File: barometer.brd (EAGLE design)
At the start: 58.4 x 40.4 mm, 103 parts, among them IC1 TPS5410, IC2 ZPA2326-0311A-R, IC3 MIC5225-3.3v, Q1 BC817, U1 LTC2850, U2 PCA9306, U3 DAC8574, U4 XTR117, U5 XC6215XC6215B182NR, U6 MAX3221, U7 Tiny85-20-SMT, X1 1751248, X2 1751264

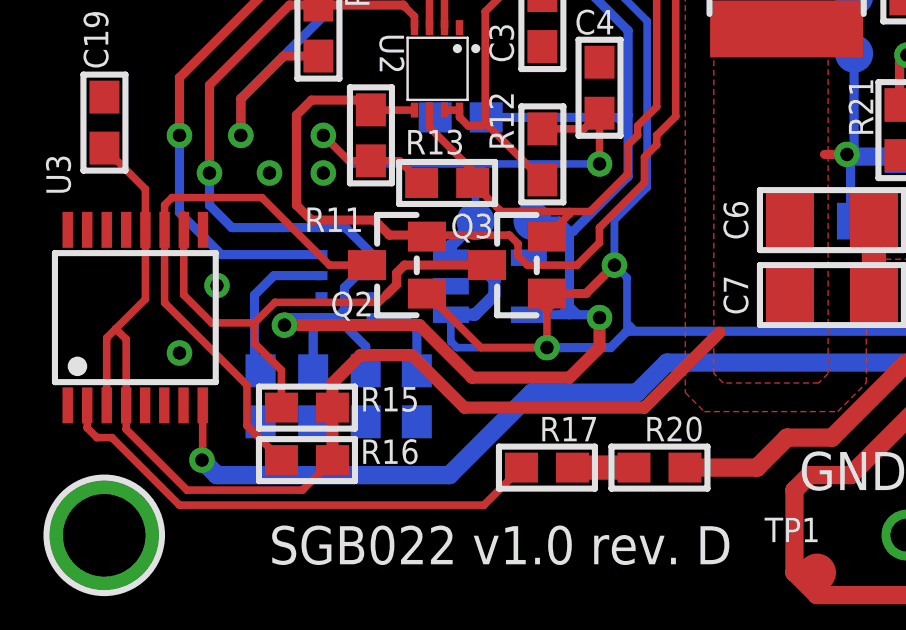
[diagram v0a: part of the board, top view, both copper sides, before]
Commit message: Optimize via placement and routing
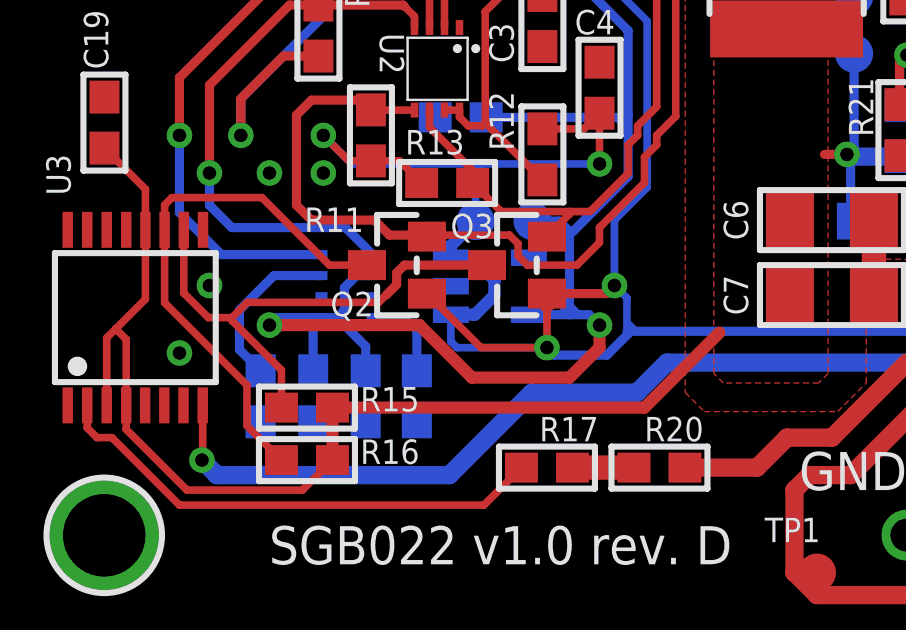
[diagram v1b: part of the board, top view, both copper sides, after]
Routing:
- net +5V0: track 47.2 -> 45.2 mm
- net +1V8: track 80.4 -> 81.3 mm
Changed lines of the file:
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@@
 <via x="17.4025" y="23.0825" extent="1-16" drill="0.45"/>
 <via x="54.88" y="6.7525" extent="1-16" drill="0.45"/>
-<via x="7.25" y="11.82" extent="1-16" drill="0.45"/>
+<via x="7" y="11.82" extent="1-16" drill="0.45"/>
 </signal>
 <signal name="+5V0">
@@
 <contactref element="R16" pad="2"/>
 <contactref element="R15" pad="2"/>
-<wire x1="13.75" y1="9.5" x2="15.5" y2="7.75" width="0.4064" layer="1"/>
-<wire x1="15.5" y1="7.75" x2="21.5" y2="7.75" width="0.4064" layer="1"/>
-<wire x1="21.5" y1="7.75" x2="24" y2="10.25" width="0.4064" layer="1"/>
-<wire x1="13.75" y1="9.5" x2="12.035" y2="9.5" width="0.4064" layer="1"/>
+<wire x1="24" y1="10.25" x2="21.5" y2="7.75" width="0.4064" layer="1"/>
 <wire x1="30.0075" y1="16.1175" x2="28.3225" y2="16.1175" width="0.6096" layer="16"/>
 <wire x1="28.3225" y1="16.1175" x2="28.25" y2="16.19" width="0.6096" layer="16"/>
@@
 <contactref element="U3" pad="4"/>
 <contactref element="C19" pad="1"/>
-<wire x1="12.035" y1="9.5" x2="11.1" y2="8.565" width="0.4064" layer="1"/>
-<wire x1="11.1" y1="8.565" x2="11.1" y2="7.75" width="0.4064" layer="1"/>
 <wire x1="11.1" y1="7.75" x2="11.1" y2="6" width="0.4064" layer="1"/>
 <wire x1="4.865" y1="13.675" x2="4.865" y2="11.365" width="0.254" layer="1"/>
@@
 <wire x1="3.5" y1="16.4" x2="4.865" y2="15.035" width="0.254" layer="1"/>
 <wire x1="4.865" y1="15.035" x2="4.865" y2="13.675" width="0.254" layer="1"/>
+<wire x1="21.5" y1="7.75" x2="11.1" y2="7.75" width="0.4064" layer="1"/>
 </signal>
 <signal name="B1">
@@
 <wire x1="16.1925" y1="26.25" x2="16.1925" y2="26.4897" width="0.254" layer="16"/>
 <wire x1="16.6225" y1="24.3775" x2="16.1925" y2="24.8075" width="0.254" layer="16"/>
-<wire x1="18.25" y1="11.55" x2="19.55" y2="11.55" width="0.3048" layer="1"/>
-<wire x1="19.55" y1="11.55" x2="20.5" y2="12.5" width="0.3048" layer="1"/>
-<via x="20.5" y="12.5" extent="1-16" drill="0.45"/>
+<via x="20.5" y="11.82" extent="1-16" drill="0.45"/>
 <wire x1="12.5" y1="28.5" x2="13.5" y2="27.5" width="0.3048" layer="16"/>
 <wire x1="15.1822" y1="27.5" x2="16.1925" y2="26.4897" width="0.3048" layer="16"/>
 <wire x1="13.5" y1="27.5" x2="15.1822" y2="27.5" width="0.3048" layer="16"/>
-<wire x1="18.25" y1="9.75" x2="20.375" y2="9.75" width="0.3048" layer="16"/>
-<wire x1="20.375" y1="9.75" x2="20.875" y2="10.25" width="0.3048" layer="16"/>
-<wire x1="20.875" y1="10.25" x2="20.9175" y2="10.2925" width="0.3048" layer="16"/>
 <wire x1="21.59" y1="20.635" x2="21.59" y2="15.09" width="0.254" layer="16"/>
 <wire x1="21.59" y1="15.09" x2="20.5" y2="14" width="0.254" layer="16"/>
-<wire x1="20.5" y1="14" x2="20.5" y2="12.5" width="0.254" layer="16"/>
-<wire x1="20.5" y1="12.5" x2="20.9175" y2="12.0825" width="0.254" layer="16"/>
-<wire x1="20.9175" y1="12.0825" x2="20.9175" y2="10.2925" width="0.254" layer="16"/>
 <wire x1="21" y1="10.5" x2="21.125" y2="10.375" width="0.254" layer="16"/>
-<wire x1="21" y1="10.5" x2="21" y2="10.375" width="0.254" layer="16"/>
-<wire x1="21" y1="10.375" x2="20.875" y2="10.25" width="0.254" layer="16"/>
+<wire x1="21" y1="10.375" x2="21" y2="10.5" width="0.254" layer="16"/>
 <contactref element="U1" pad="8"/>
 <contactref element="R2" pad="2"/>
@@
 <wire x1="14.85" y1="26.25" x2="16.1925" y2="26.25" width="0.8128" layer="16"/>
 <wire x1="40" y1="31.4" x2="40" y2="30.16" width="0.6096" layer="1"/>
+<wire x1="20.23" y1="11.55" x2="20.5" y2="11.82" width="0.3048" layer="1"/>
+<wire x1="18.25" y1="11.55" x2="20.23" y2="11.55" width="0.3048" layer="1"/>
+<wire x1="20.5" y1="14" x2="20.5" y2="11.82" width="0.254" layer="16"/>
+<wire x1="20.9175" y1="10.2925" x2="20.9175" y2="11.4025" width="0.254" layer="16"/>
+<wire x1="20.9175" y1="11.4025" x2="20.5" y2="11.82" width="0.254" layer="16"/>
+<wire x1="18.25" y1="9.75" x2="18.5" y2="9.5" width="0.3048" layer="16"/>
+<wire x1="18.5" y1="9.5" x2="20.25" y2="9.5" width="0.3048" layer="16"/>
+<wire x1="21" y1="10.25" x2="21" y2="10.375" width="0.3048" layer="16"/>
+<wire x1="20.25" y1="9.5" x2="21" y2="10.25" width="0.3048" layer="16"/>
 </signal>
 <signal name="C1+">
@@
 <wire x1="12.2084" y1="8.9762" x2="12.2084" y2="9.7916" width="0.3048" layer="16"/>
 <wire x1="12.2084" y1="9.7916" x2="11.25" y2="10.75" width="0.3048" layer="16"/>
-<via x="20.0025" y="10.75" extent="1-16" drill="0.45"/>
-<via x="9.5" y="10.5" extent="1-16" drill="0.45"/>
-<wire x1="9.5" y1="10.5" x2="9.75" y2="10.75" width="0.3048" layer="16"/>
-<wire x1="9.75" y1="10.75" x2="10.735" y2="10.75" width="0.3048" layer="16"/>
+<via x="20.0025" y="10.5" extent="1-16" drill="0.45"/>
+<via x="9" y="10.5" extent="1-16" drill="0.45"/>
+<wire x1="9" y1="10.5" x2="9.25" y2="10.75" width="0.3048" layer="16"/>
+<wire x1="9.25" y1="10.75" x2="10.735" y2="10.75" width="0.3048" layer="16"/>
 <contactref element="U2" pad="2"/>
 <wire x1="14.835" y1="20.4175" x2="14.835" y2="22.035" width="0.254" layer="1"/>
@@
 <wire x1="9.4675" y1="19.4675" x2="10.6325" y2="19.4675" width="0.3048" layer="1"/>
 <wire x1="14" y1="10.5" x2="15.75" y2="8.75" width="0.4064" layer="1"/>
-<wire x1="14" y1="10.5" x2="9.5" y2="10.5" width="0.4064" layer="1"/>
+<wire x1="14" y1="10.5" x2="9" y2="10.5" width="0.4064" layer="1"/>
 <wire x1="17.6475" y1="10.8475" x2="19" y2="10.8475" width="0.3048" layer="16"/>
 <wire x1="17.7725" y1="13.9675" x2="18.6575" y2="13.9675" width="0.3048" layer="16"/>
@@
 <wire x1="19" y1="11.125" x2="18.75" y2="10.875" width="0.3048" layer="16"/>
 <wire x1="19" y1="11.125" x2="19.25" y2="10.875" width="0.3048" layer="16"/>
-<wire x1="20.0025" y1="9.7525" x2="20.0025" y2="10.75" width="0.4064" layer="1"/>
 <wire x1="15.75" y1="8.75" x2="19" y2="8.75" width="0.4064" layer="1"/>
 <wire x1="19" y1="8.75" x2="20.0025" y2="9.7525" width="0.4064" layer="1"/>
 <wire x1="20.955" y1="17.5" x2="20.955" y2="15.455" width="0.3048" layer="16"/>
-<wire x1="19.905" y1="10.8475" x2="20.0025" y2="10.75" width="0.3048" layer="16"/>
-<wire x1="19" y1="10.8475" x2="19.905" y2="10.8475" width="0.3048" layer="16"/>
+<wire x1="19" y1="10.8475" x2="19.655" y2="10.8475" width="0.3048" layer="16"/>
 <wire x1="11.1125" y1="21.5875" x2="9.7275" y2="22.9725" width="0.3048" layer="16"/>
 <wire x1="9.7275" y1="22.9725" x2="9.7275" y2="25.5875" width="0.3048" layer="16"/>
@@
 <wire x1="19.125" y1="13.625" x2="19" y2="13.625" width="0.3048" layer="16"/>
 <wire x1="20.955" y1="15.455" x2="19.125" y2="13.625" width="0.3048" layer="16"/>
+<wire x1="20.0025" y1="9.7525" x2="20.0025" y2="10.5" width="0.4064" layer="1"/>
+<wire x1="19.655" y1="10.8475" x2="20.0025" y2="10.5" width="0.3048" layer="16"/>
 </signal>
 <signal name="VREF_3V3">
@@
 <contactref element="IC2" pad="3"/>
 <contactref element="R19" pad="1"/>
-<wire x1="10.735" y1="12.15" x2="9.15" y2="12.15" width="0.3048" layer="16"/>
-<wire x1="9.15" y1="12.15" x2="8.5" y2="11.5" width="0.3048" layer="16"/>
-<wire x1="8.5" y1="11.5" x2="8.5" y2="9.1823" width="0.3048" layer="16"/>
-<wire x1="8.5" y1="9.1823" x2="8.7061" y2="8.9762" width="0.3048" layer="16"/>
+<wire x1="9.15" y1="12.15" x2="10.735" y2="12.15" width="0.3048" layer="16"/>
+<wire x1="8.7061" y1="8.9762" x2="8" y2="9.6823" width="0.3048" layer="16"/>
+<wire x1="8" y1="11" x2="9.15" y2="12.15" width="0.3048" layer="16"/>
+<wire x1="8" y1="9.6823" x2="8" y2="11" width="0.3048" layer="16"/>
 </signal>
 <signal name="VREF">
@@
 <contactref element="U3" pad="10"/>
 <wire x1="9.4" y1="7.75" x2="9.4" y2="9" width="0.254" layer="1"/>
-<wire x1="6.145" y1="13.675" x2="6.145" y2="11.50158125" width="0.254" layer="1"/>
-<wire x1="6.145" y1="11.50158125" x2="7.073290625" y2="10.573290625" width="0.254" layer="1"/>
-<wire x1="7.073290625" y1="10.573290625" x2="8.500746875" y2="10.573290625" width="0.254" layer="1"/>
-<wire x1="8.500746875" y1="10.573290625" x2="9.18585625" y2="11.2584" width="0.254" layer="1"/>
 <wire x1="12.64629375" y1="11.2584" x2="12.88789375" y2="11.5" width="0.254" layer="1"/>
-<wire x1="9.18585625" y1="11.2584" x2="12.64629375" y2="11.2584" width="0.254" layer="1"/>
-<wire x1="9.4" y1="9" x2="8.500746875" y2="9.899253125" width="0.254" layer="1"/>
-<wire x1="8.500746875" y1="9.899253125" x2="8.500746875" y2="10.573290625" width="0.254" layer="1"/>
+<wire x1="6.145" y1="13.675" x2="6.145" y2="11.5665375" width="0.254" layer="1"/>
+<wire x1="6.145" y1="11.5665375" x2="6.9615375" y2="10.75" width="0.254" layer="1"/>
+<wire x1="6.9615375" y1="10.75" x2="7.75" y2="10.75" width="0.254" layer="1"/>
+<wire x1="7.75" y1="10.75" x2="8.2584" y2="11.2584" width="0.254" layer="1"/>
+<wire x1="8.2584" y1="11.2584" x2="12.64629375" y2="11.2584" width="0.254" layer="1"/>
+<wire x1="9.4" y1="9" x2="7.75" y2="10.65" width="0.254" layer="1"/>
+<wire x1="7.75" y1="10.65" x2="7.75" y2="10.75" width="0.254" layer="1"/>
 </signal>
 <signal name="I-IN">

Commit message: Fix feedback resistance in +5V0 buck converter
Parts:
- R14: value 3.16k -> 3.01k
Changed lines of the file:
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@@
 <attribute name="NAME" x="29.127" y="16.778" size="0.8128" layer="26" font="vector" ratio="18" rot="MR90" align="top-left"/>
 </element>
-<element name="R14" library="microbuilder" package="0603" value="3.16k" x="32.0675" y="13.9675" smashed="yes" rot="R180">
+<element name="R14" library="microbuilder" package="0603" value="3.01k" x="32.0675" y="13.9675" smashed="yes" rot="R180">
 <attribute name="NAME" x="30.409" y="12.2095" size="0.8128" layer="25" font="vector" ratio="18"/>
 </element>

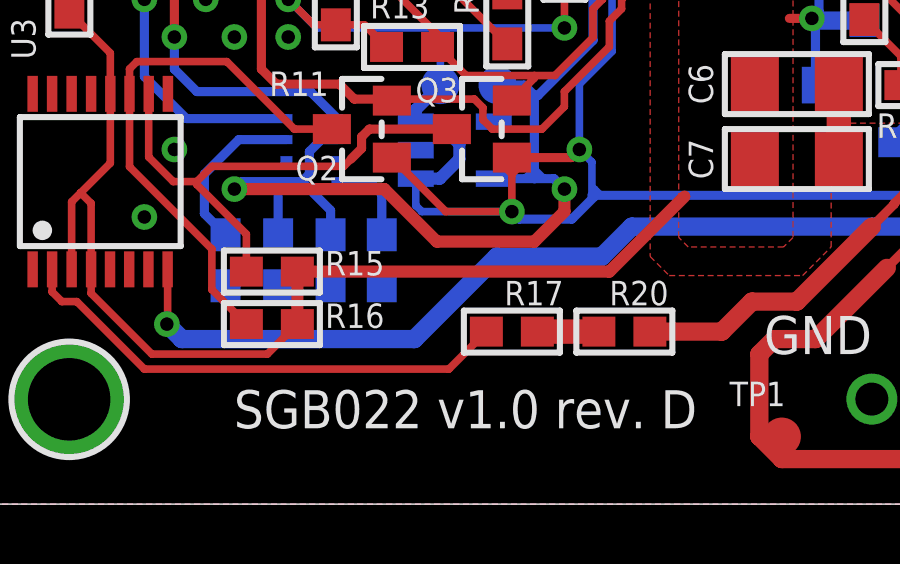
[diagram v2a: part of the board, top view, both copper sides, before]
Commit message: Add test point for DAC output corresponding to 4-20 mA current loop
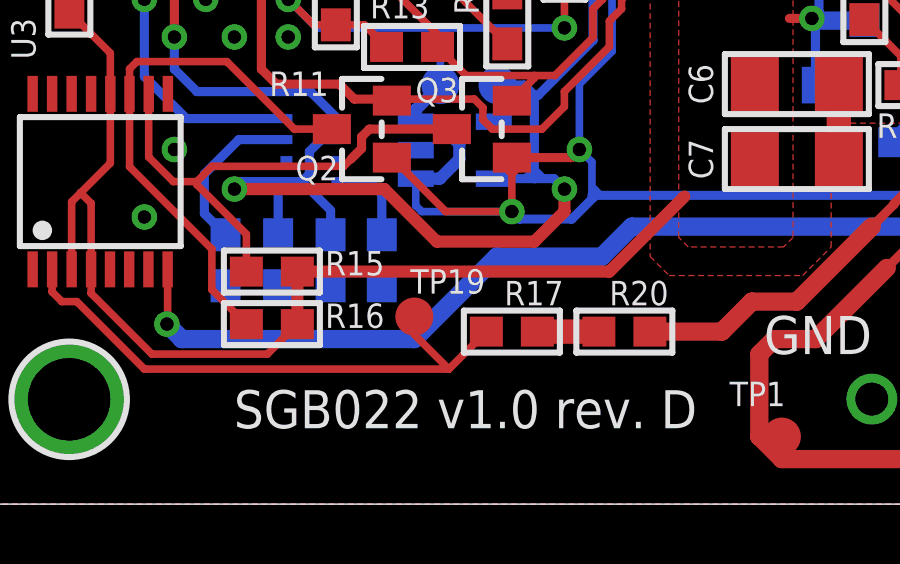
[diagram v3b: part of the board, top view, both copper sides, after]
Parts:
- added TP19: PTR1B1,27, testpad:B1,27
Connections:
- net V-OUT-2: now also TP19.TP
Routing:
- net V-OUT-2: track 16.8 -> 19.0 mm
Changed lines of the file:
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@@
 <attribute name="NAME" x="12.722" y="27.123" size="0.8128" layer="26" font="vector" ratio="18" rot="MR90"/>
+</element>
+<element name="TP19" library="testpad" library_urn="urn:adsk.eagle:library:385" package="B1,27" package3d_urn="urn:adsk.eagle:package:27944/1" value="PTR1B1,27" x="15" y="6.25" smashed="yes">
+<attribute name="NAME" x="14.865" y="7.016" size="0.8128" layer="25" font="vector" ratio="18"/>
+<attribute name="TP_SIGNAL_NAME" value="" x="15" y="6.25" size="1.778" layer="27" display="off"/>
 </element>
 </elements>
@@
 <wire x1="6" y1="4.5" x2="16.15" y2="4.5" width="0.254" layer="1"/>
 <wire x1="16.15" y1="4.5" x2="17.4" y2="5.75" width="0.254" layer="1"/>
+<contactref element="TP19" pad="TP"/>
+<wire x1="15" y1="6.25" x2="15" y2="5.65" width="0.254" layer="1"/>
+<wire x1="15" y1="5.65" x2="16.15" y2="4.5" width="0.254" layer="1"/>
 </signal>
 </signals>

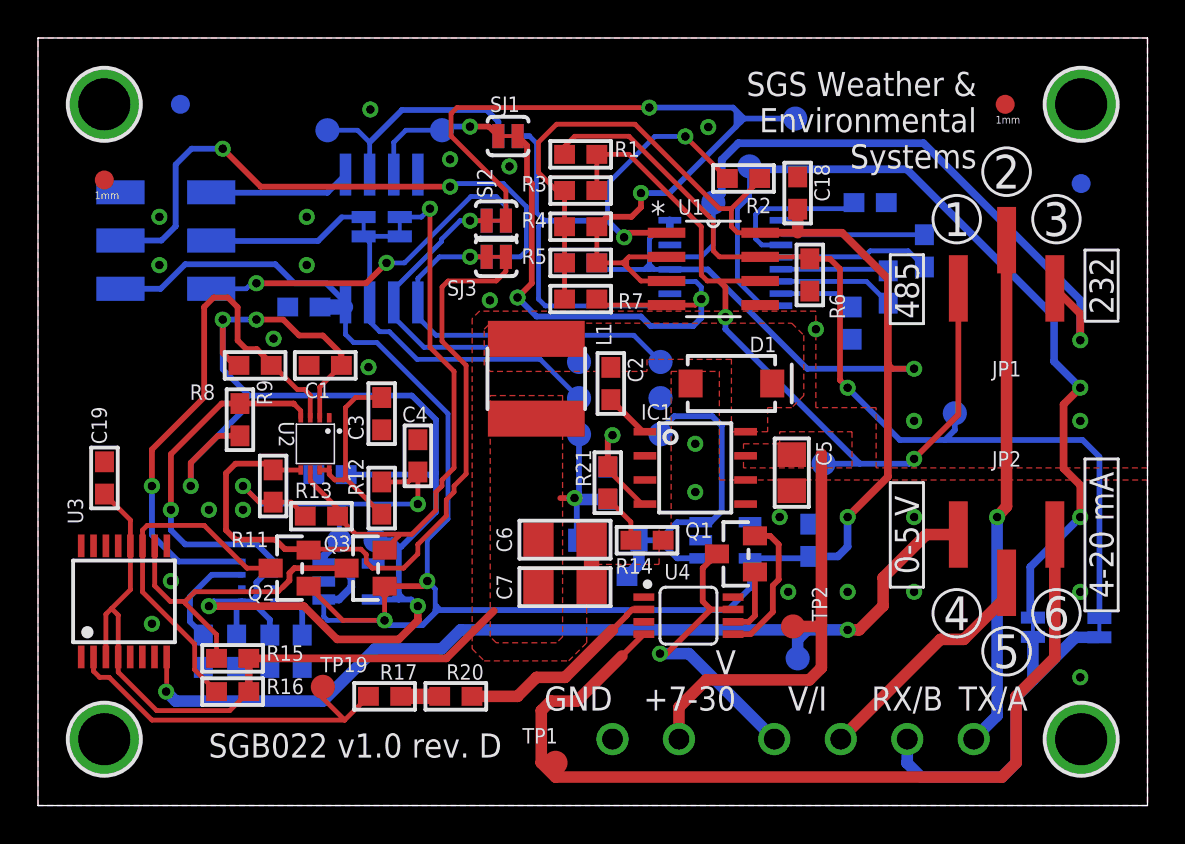
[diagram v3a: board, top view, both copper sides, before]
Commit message: Add additional jumper for analog output format
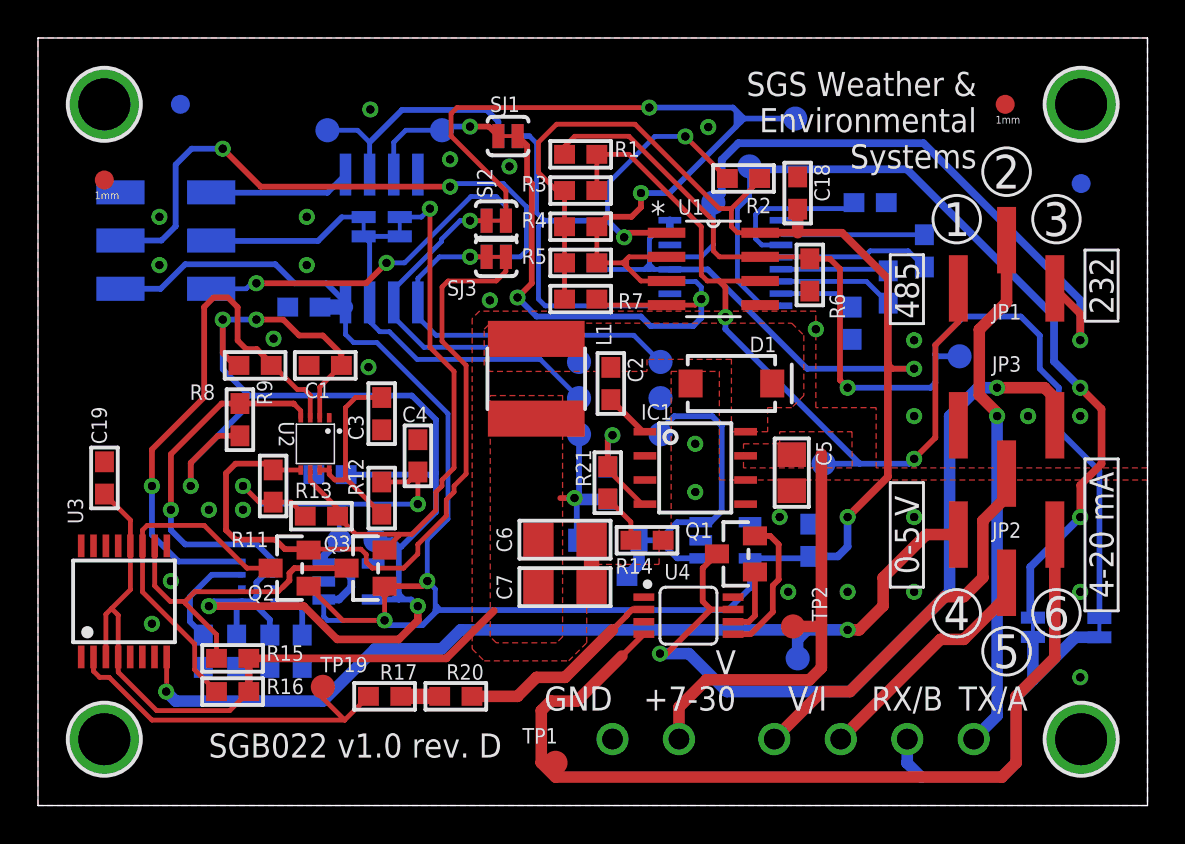
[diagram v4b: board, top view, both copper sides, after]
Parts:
- added JP3: Analog Output Format 2, microbuilder:1X03_SMT
- JP2: value Analog Output Format -> Analog Output Format 1
- moved TP11 3.01 mm to (48.5, 23.7)
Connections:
- new net A-OUT-2: JP3.2, X2.4
- net COLLECTOR: now also JP3.3; no longer X2.4
- net GND: now also JP3.1
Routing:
- net COLLECTOR: track 16.1 -> 43.6 mm, vias 1 -> 2
- net A-OUT-2: track 0.00 -> 20.5 mm
- net B: track 50.3 -> 56.1 mm
- net D-OUT-2: track 27.0 -> 27.8 mm
- net GND: vias 27 -> 29
